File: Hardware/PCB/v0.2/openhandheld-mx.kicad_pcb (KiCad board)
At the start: 2 copper layers, 80 x 40 mm, 11 parts

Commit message: PCB v0.2: Completed schematic
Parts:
- removed the REF** at (19.8, -15.5)
- removed the REF** at (-30.0, -15.5)
- removed the REF** at (27.5, 1.00)
- removed the REF** at (-20.0, 16.0)
- removed the REF** at (20.0, 16.0)
- removed the REF** at (35.0, -15.0)
- removed the REF** at (-35.0, -15.0)
- removed the REF** at (0.00, 0.00)
- removed the S? at (33.5, -2.50)
- removed the S? at (23.5, 2.50)
- removed the VR at (-28.5, 0.00)
- added REF**: SJ-3524-SMT-TR, _AKL_Connector:SJ-3524-SMT-TR, B.Cu at (-12.0, -12.5)
- added REF**: MountingHole_2.2mm_M2_Pad, MountingHole:MountingHole_2.2mm_M2_Pad, F.Cu at (37.0, -16.0)
- added REF**: MountingHole_2.2mm_M2_Pad, MountingHole:MountingHole_2.2mm_M2_Pad, F.Cu at (20.5, 16.0)
- added REF**: MountingHole_2.2mm_M2_Pad, MountingHole:MountingHole_2.2mm_M2_Pad, F.Cu at (-20.5, 16.0)
- added REF**: MountingHole_2.2mm_M2_Pad, MountingHole:MountingHole_2.2mm_M2_Pad, F.Cu at (-37.0, -16.0)
- added REF**: PinSocket_2x05_P2.54mm_Vertical, Connector_PinSocket_2.54mm:PinSocket_2x05_P2.54mm_Vertical, F.Cu at (-30.1, -19.0)
- added REF**: Speaker_15x11mm, _AKL_Speaker:Speaker_15x11mm, B.Cu at (-32.5, 10.0)
- added REF**: ST7789_1.54_240x240, _AKL_Display:ST7789_1.54_240x240, F.Cu at (0.00, 0.00)
- added REF**: DFN-8-1EP_6x5mm_P1.27mm_EP2x2mm, Package_DFN_QFN:DFN-8-1EP_6x5mm_P1.27mm_EP2x2mm, B.Cu at (0.00, 8.50)
- added REF**: STM32-UFQFPN48, _AKL_IC:STM32-UFQFPN48, B.Cu at (0.00, 0.00)
- added REF**: PinSocket_2x06_P2.54mm_Vertical, Connector_PinSocket_2.54mm:PinSocket_2x06_P2.54mm_Vertical, F.Cu at (19.0, -26.0)
- added REF**: PinSocket_2x05_P2.54mm_Vertical, Connector_PinSocket_2.54mm:PinSocket_2x05_P2.54mm_Vertical, F.Cu at (19.9, -19.0)
- added REF**: BK-880, _AKL_Battery:BK-880, B.Cu at (29.0, 0.00)
- added S?: Button-SMD-6x6, _AKL_Switch:Button-SMD-6x6-Cap, F.Cu at (34.0, -2.50)
- added S?: Button-SMD-6x6, _AKL_Switch:Button-SMD-6x6-Cap, F.Cu at (24.0, 2.50)
- added VR: FJ08K-N, _AKL_ResistorVar:FJ08K-N, F.Cu at (-29.0, 0.00)
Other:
- board size 80 x 40 mm -> 84 x 42 mm
- board text added: "ONLY LIR2450"
- board text removed: "Dejar hueco en el acrilico para la pestaña central del conector SWD, como en la de nano 0"

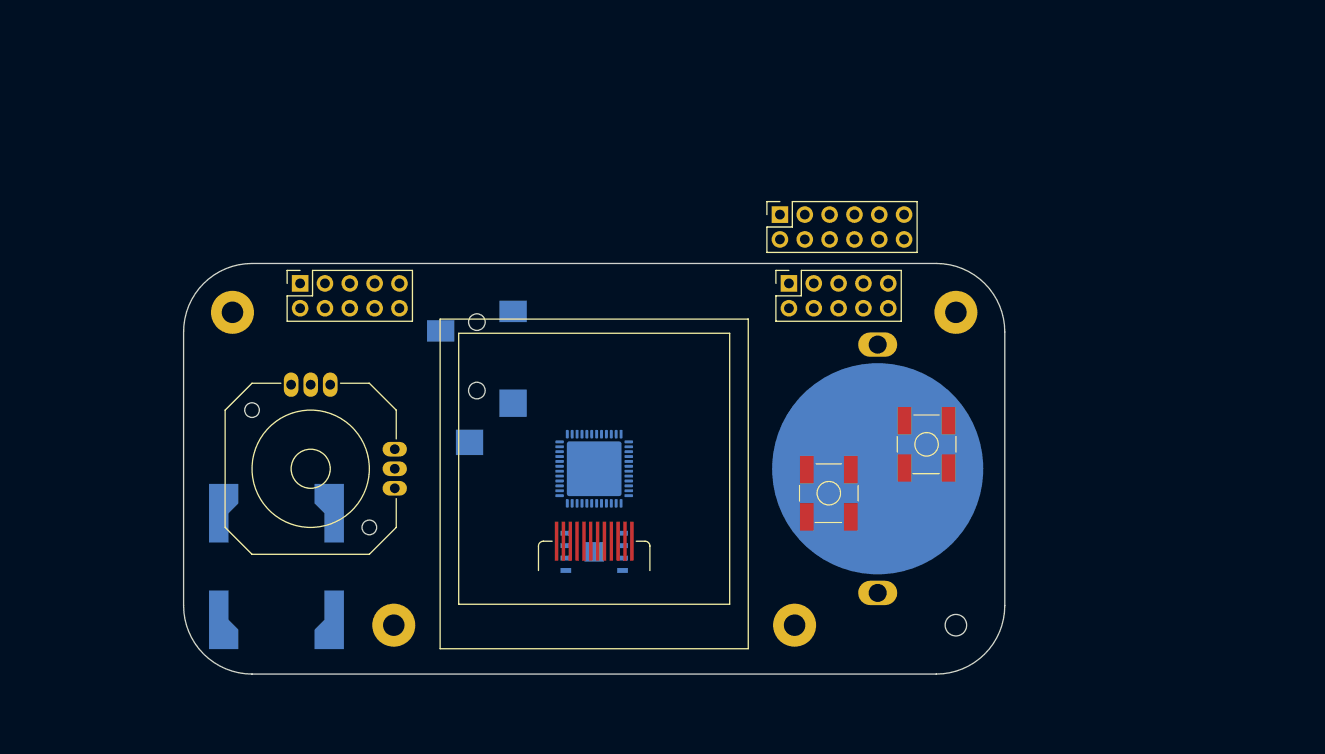
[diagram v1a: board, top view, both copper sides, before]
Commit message: PCB v0.2: Reduced component dimensions. Preliminary placement
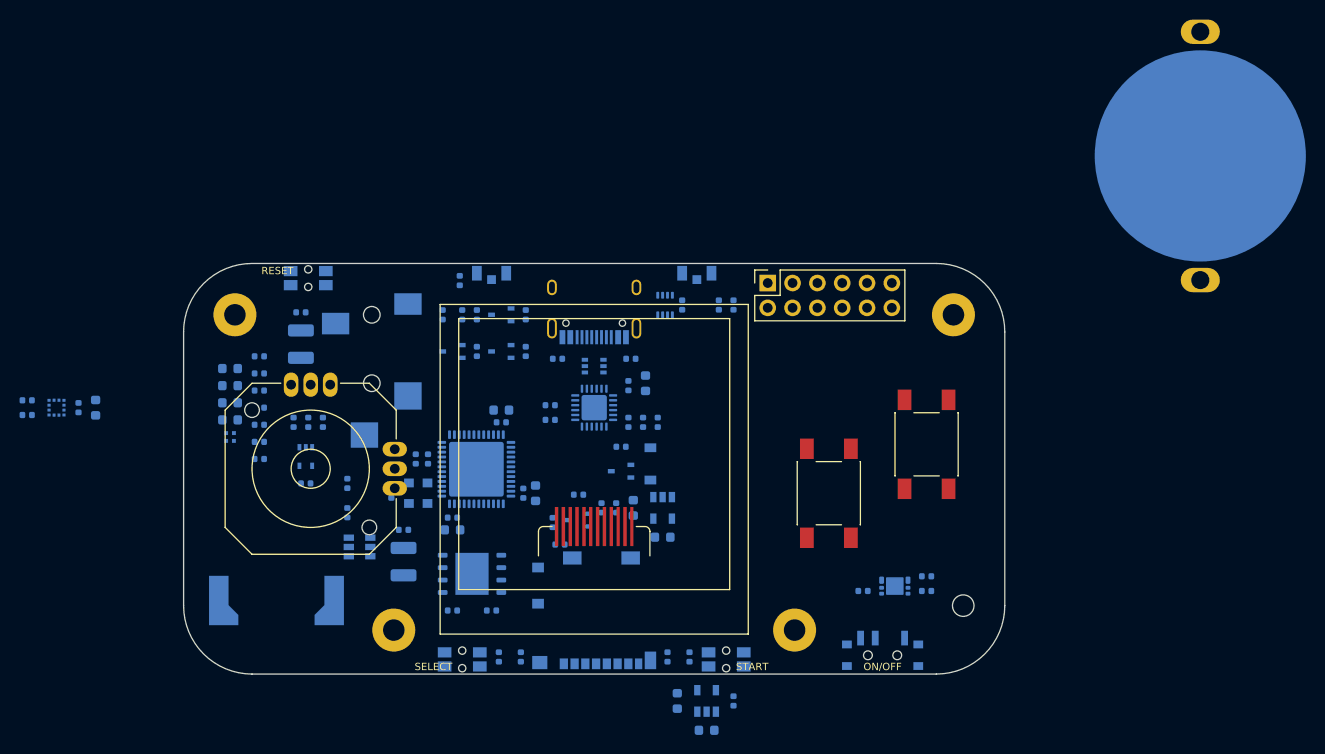
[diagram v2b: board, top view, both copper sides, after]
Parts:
- removed the REF** at (-12.0, -12.5)
- removed the REF** at (37.0, -16.0)
- removed the REF** at (20.5, 16.0)
- removed the REF** at (-30.1, -19.0)
- removed the REF** at (-32.5, 10.0)
- removed the REF** at (0.00, 0.00) (x2)
- removed the REF** at (0.00, 8.50)
- removed the REF** at (19.0, -26.0)
- removed the REF** at (19.9, -19.0)
- removed the REF** at (29.0, 0.00)
- removed S? (x2): Button-SMD-6x6, _AKL_Switch:Button-SMD-6x6-Cap
- removed VR: FJ08K-N, _AKL_ResistorVar:FJ08K-N
- added C1: 10uF, Capacitor_SMD:C_0603_1608Metric, B.Cu at (5.25, -8.75)
- added C10: 1uF, Capacitor_SMD:C_0402_1005Metric, B.Cu at (-18.2, -1.00)
- added C11: 100nF, Capacitor_SMD:C_0402_1005Metric, B.Cu at (-20.8, 2.50)
- added C12: 100nF, Capacitor_SMD:C_0402_1005Metric, B.Cu at (-17.0, -1.00)
- added C13: 10uF, Capacitor_SMD:C_0603_1608Metric, B.Cu at (-9.50, -6.00)
- added C14: 10uF, Capacitor_SMD:C_0603_1608Metric, B.Cu at (11.5, 26.8)
- added C15: 100nF, Capacitor_SMD:C_0402_1005Metric, B.Cu at (-9.50, -4.75)
- added C16: 1uF, Capacitor_SMD:C_0402_1005Metric, B.Cu at (-19.5, 6.25)
- added C17: 10uF, Capacitor_SMD:C_0603_1608Metric, B.Cu at (-6.00, 2.50)
- added C18: 100uF, Capacitor_SMD:C_1210_3225Metric, B.Cu at (-19.5, 9.50)
- added C19: 100nF, Capacitor_SMD:C_0402_1005Metric, B.Cu at (-7.25, 2.50)
- added C2: 100nF, Capacitor_SMD:C_0402_1005Metric, B.Cu at (3.50, -8.50)
- added C20: 10uF, Capacitor_SMD:C_0603_1608Metric, B.Cu at (-14.5, 6.25)
- added C21: 100nF, Capacitor_SMD:C_0402_1005Metric, B.Cu at (-14.5, 5.00)
- added C22: 100nF, Capacitor_SMD:C_0402_1005Metric, B.Cu at (34.0, 12.5)
- added C23: 10uF, Capacitor_SMD:C_0603_1608Metric, B.Cu at (-51.0, -6.25)
- added C24: 100nF, Capacitor_SMD:C_0402_1005Metric, B.Cu at (-52.8, -6.25)
- added C25: 100nF, Capacitor_SMD:C_0402_1005Metric, B.Cu at (-10.5, 14.5)
- added C26: 10uF, Capacitor_SMD:C_0603_1608Metric, B.Cu at (4.00, 4.00)
- added C27: 100nF, Capacitor_SMD:C_0402_1005Metric, B.Cu at (7.50, 19.2)
- added C28: 10uF, Capacitor_SMD:C_0603_1608Metric, B.Cu at (7.00, 7.00)
- added C29: 100nF, Capacitor_SMD:C_0402_1005Metric, B.Cu at (-4.25, 5.50)
- added C3: 100nF, Capacitor_SMD:C_0402_1005Metric, B.Cu at (-29.5, 1.50)
- added C4: 100nF, Capacitor_SMD:C_0402_1005Metric, B.Cu at (-13.5, -15.8)
- added C5: 100nF, Capacitor_SMD:C_0402_1005Metric, B.Cu at (-27.8, -4.75)
- added C6: 100uF, Capacitor_SMD:C_1210_3225Metric, B.Cu at (-30.0, -12.8)
- added C7: 10uF, Capacitor_SMD:C_0603_1608Metric, B.Cu at (8.50, 23.8)
- added C8: 100nF, Capacitor_SMD:C_0402_1005Metric, B.Cu at (-25.2, 1.50)
- added C9: 1uF, Capacitor_SMD:C_0402_1005Metric, B.Cu at (9.00, -16.8)
- added D1: PESD5V0L5UY, Package_TO_SOT_SMD:SOT-363_SC-70-6, B.Cu at (0.00, -10.5)
- added D2: BLUE, LED_SMD:LED_0603_1608Metric, B.Cu at (-37.2, -5.00)
- added D3: BLUE, LED_SMD:LED_0603_1608Metric, B.Cu at (-37.2, -6.75)
- added D4: RED, LED_SMD:LED_0603_1608Metric, B.Cu at (-37.2, -8.50)
- added D5: VEMD10940F, _AKL_Optical:Vishay_IR, B.Cu at (10.5, -20.0)
- added D6: VSMB10940, _AKL_Optical:Vishay_IR, B.Cu at (-10.5, -20.0)
- added D7: RGB, _AKL_Optical:150044M155260, B.Cu at (-37.2, -3.25)
- added D8: MBR0520L, Diode_SMD:D_SOD-123, B.Cu at (5.75, -0.50)
- added D9: GREEN, LED_SMD:LED_0603_1608Metric, B.Cu at (-37.2, -10.2)
- added DS1: ST7789_1.54_240x240, _AKL_Display:ST7789_1.54_240x240, F.Cu at (0.00, -1.50)
- added J1: TYPE-C-31-M-12, _AKL_Connector:TYPE-C-31-M-12, B.Cu at (0.00, -17.5)
- added J2: SJ-3524-SMT-TR, _AKL_Connector:SJ-3524-SMT-TR, B.Cu at (-22.8, -13.2)
- added J3: BK-880, _AKL_Battery:BK-880, B.Cu at (62.0, -32.0)
- added J4: 1040310811, _AKL_Connector:1040310811, B.Cu at (0.00, 14.5)
- added J5: PPPC062LFBN-RC, Connector_PinSocket_2.54mm:PinSocket_2x06_P2.54mm_Vertical, F.Cu at (17.8, -19.0)
- added LS1: CMS-151125-078S, _AKL_Speaker:Speaker_15x11mm, B.Cu at (-32.5, 8.50)
- added Q1: SI2102-TP, Package_TO_SOT_SMD:SOT-323_SC-70, B.Cu at (-9.50, -12.0)
- added Q2: SI2102-TP, Package_TO_SOT_SMD:SOT-323_SC-70, B.Cu at (-9.50, -15.8)
- added Q3: SI2102-TP, Package_TO_SOT_SMD:SOT-323_SC-70, B.Cu at (-14.5, -12.0)
- added Q4: SI2101-TP, Package_TO_SOT_SMD:SOT-323_SC-70, B.Cu at (2.75, 0.25)
- added Q5: SI2102-TP, Package_TO_SOT_SMD:SOT-323_SC-70, B.Cu at (-1.80, 5.25)
- added R1: 20K, Resistor_SMD:R_0402_1005Metric, B.Cu at (-7.00, -15.8)
- added R10: 20K, Resistor_SMD:R_0402_1005Metric, B.Cu at (-15.5, -15.8)
- added R11: 1K8, Resistor_SMD:R_0402_1005Metric, B.Cu at (-34.2, -6.25)
- added R12: 1K8, Resistor_SMD:R_0402_1005Metric, B.Cu at (-30.0, -16.0)
- added R13: 1K8, Resistor_SMD:R_0402_1005Metric, B.Cu at (-34.2, -8.00)
- added R14: 2K4, Resistor_SMD:R_0402_1005Metric, B.Cu at (-34.2, -9.75)
- added R15: 120K, Resistor_SMD:R_0402_1005Metric, B.Cu at (-25.2, 4.50)
- added R16: 20K, Resistor_SMD:R_0402_1005Metric, B.Cu at (14.2, 23.8)
- added R17: 5K1, Resistor_SMD:R_0402_1005Metric, B.Cu at (-4.50, -5.00)
- added R18: 150, Resistor_SMD:R_0402_1005Metric, B.Cu at (-13.8, -19.2)
- added R19: 5K1, Resistor_SMD:R_0402_1005Metric, B.Cu at (-4.50, -6.50)
- added R2: 20K, Resistor_SMD:R_0402_1005Metric, B.Cu at (-7.00, -12.0)
- added R20: 510, Resistor_SMD:R_0402_1005Metric, B.Cu at (34.0, 11.0)
- added R21: 2K4, Resistor_SMD:R_0402_1005Metric, B.Cu at (27.5, 12.5)
- added R22: 240, Resistor_SMD:R_0402_1005Metric, B.Cu at (-34.2, -4.50)
- added R23: 1K8, Resistor_SMD:R_0402_1005Metric, B.Cu at (-34.2, -2.75)
- added R24: 1K, Resistor_SMD:R_0402_1005Metric, B.Cu at (-34.2, -1.00)
- added R25: 120K, Resistor_SMD:R_0402_1005Metric, B.Cu at (2.75, -2.25)
- added R26: 20K, Resistor_SMD:R_0402_1005Metric, B.Cu at (-14.5, 14.5)
- added R27: 5K1, Resistor_SMD:R_0402_1005Metric, B.Cu at (-58.0, -5.50)
- added R28: 5K1, Resistor_SMD:R_0402_1005Metric, B.Cu at (-58.0, -7.00)
- added R29: 20K, Resistor_SMD:R_0402_1005Metric, B.Cu at (-7.50, 19.2)
- added R3: 1K, Resistor_SMD:R_0402_1005Metric, B.Cu at (3.50, -4.75)
- added R30: 20K, Resistor_SMD:R_0402_1005Metric, B.Cu at (-1.60, 2.65)
- added R31: 100, Resistor_SMD:R_0402_1005Metric, B.Cu at (-3.50, 7.75)
- added R32: 510, Resistor_SMD:R_0402_1005Metric, B.Cu at (-34.2, -11.5)
- added R33: 20K, Resistor_SMD:R_0402_1005Metric, B.Cu at (14.2, -16.8)
- added R34: 20K, Resistor_SMD:R_0402_1005Metric, B.Cu at (12.8, -16.8)
- added R35: 20K, Resistor_SMD:R_0402_1005Metric, B.Cu at (9.75, 19.2)
- added R36: 75K, Resistor_SMD:R_0402_1005Metric, B.Cu at (6.50, -4.75)
- added R37: 120K, Resistor_SMD:R_0402_1005Metric, B.Cu at (5.00, -4.75)
- added R38: 20K, Resistor_SMD:R_0402_1005Metric, B.Cu at (-9.75, 19.2)
- added R39: 75K, Resistor_SMD:R_0402_1005Metric, B.Cu at (2.25, 4.00)
- added R4: 5K1, Resistor_SMD:R_0402_1005Metric, B.Cu at (3.75, -11.2)
- added R40: 120K, Resistor_SMD:R_0402_1005Metric, B.Cu at (0.75, 4.00)
- added R5: 5K1, Resistor_SMD:R_0402_1005Metric, B.Cu at (-3.75, -11.2)
- added R6: 20K, Resistor_SMD:R_0402_1005Metric, B.Cu at (-12.0, -12.0)
- added R7: 20K, Resistor_SMD:R_0402_1005Metric, B.Cu at (-12.0, -15.8)
- added R8: 240, Resistor_SMD:R_0402_1005Metric, B.Cu at (-30.8, -4.75)
- added R9: 100, Resistor_SMD:R_0402_1005Metric, B.Cu at (-29.2, -4.75)
- added REF**: MountingHole_2.2mm_M2_Pad, MountingHole:MountingHole_2.2mm_M2_Pad, F.Cu at (36.8, -15.8)
- added REF**: MountingHole_2.2mm_M2_Pad, MountingHole:MountingHole_2.2mm_M2_Pad, F.Cu at (20.5, 16.5)
- added SW1: RESET, _AKL_Switch:EVQP7, B.Cu at (-29.2, -19.5)
- added SW2: ON/OFF, _AKL_Switch:CUS-12TB, B.Cu at (29.5, 18.8)
- added SW3: A, _AKL_Switch:TL3301TF160QG, F.Cu at (24.0, 2.50)
- added SW4: B, _AKL_Switch:TL3301TF160QG, F.Cu at (34.0, -2.50)
- added SW5: START, _AKL_Switch:EVQP7, B.Cu at (13.5, 19.5)
- added SW6: SELECT, _AKL_Switch:EVQP7, B.Cu at (-13.5, 19.5)
- added U1: TLV9061IDCKR, Package_TO_SOT_SMD:SOT-353_SC-70-5, B.Cu at (-29.5, -1.25)
- added U10: LIS2DE12TR, _AKL_IC:LIS2DE12TR, B.Cu at (-55.0, -6.25)
- added U11: TLV74333PDBVR, Package_TO_SOT_SMD:SOT-23-5, B.Cu at (7.00, 4.00)
- added U2: CP2102N-A02-GQFN24, Package_DFN_QFN:QFN-24-1EP_4x4mm_P0.5mm_EP2.6x2.6mm, B.Cu at (0.00, -6.25)
- added U3: MCP73831T-2ACI_OT, Package_TO_SOT_SMD:SOT-23-5, B.Cu at (11.5, 23.8)
- added U4: PAM8301AAF, Package_TO_SOT_SMD:SOT-23-6, B.Cu at (-24.0, 8.00)
- added U5: DSC6001CI1A-008.0000T, _AKL_IC:DSC60XX-3.2x2.5, B.Cu at (-18.0, 2.50)
- added U6: VSOP38338, _AKL_IC:VSOP38338, B.Cu at (7.25, -16.8)
- added U7: AP9211S-AN-HAC-7, _AKL_IC:AP9211S-AN-HAC-7, B.Cu at (30.8, 12.0)
- added U8: STM32L431CCU6, _AKL_IC:STM32-UFQFPN48, B.Cu at (-12.1, 0.05)
- added U9: W25Q64JVZPIQ, _AKL_IC:Winbond_WSON8_6x5mm, B.Cu at (-12.5, 10.8)
- added VR1: FJ08K-N, _AKL_ResistorVar:FJ08K-N, F.Cu at (-29.0, 0.00)
- moved REF** 0.50 mm to (-20.5, 16.5)
- moved REF** 0.35 mm to (-36.8, -15.8)
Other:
- outline, holes or cut-outs redrawn
- rule pad_to_mask_clearance: 0.051 -> 0
- board text added: "CHG"
- board text added: "ON/OFF"
- board text added: "PWR"
- board text added: "RESET"
- board text added: "RXD"
- board text added: "SELECT"
- board text added: "START"
- board text added: "TXD"
- board text added: "USR"

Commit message: PCB v0.2: Starting to route
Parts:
- D8: value MBR0520L -> NSR0520V2T1G; footprint Diode_SMD:D_SOD-123 -> Diode_SMD:D_SOD-523
- J3: value BK-880 -> Battery; footprint _AKL_Battery:BK-880 -> _AKL_Battery:Solder_Pad_D2
- moved J3 55.1 mm to (28.5, 11.8), turned to 180 degrees
- moved R27 44.7 mm to (-13.5, -9.25)
- moved R28 44.6 mm to (-13.5, -10.5)
- moved U10 44.1 mm to (-11.0, -9.75)
- moved C24 43.9 mm to (-9.00, -9.75)
- moved C23 43.6 mm to (-7.50, -9.75)
- moved C14 40.7 mm to (7.50, -13.8), turned to 180 degrees
- moved R16 40.3 mm to (11.8, -16.5)
- moved U3 40.3 mm to (9.25, -16.5)
- moved C7 40.3 mm to (6.50, -16.5)
- moved R30 18.0 mm to (10.2, 16.2), turned to 90 degrees
- moved Q5 14.7 mm to (8.25, 16.0), turned to 90 degrees
- moved C11 13.1 mm to (-12.2, -7.50), turned to 0 degrees
- moved R31 13.0 mm to (8.25, 13.2), turned to 270 degrees
- moved C15 10.3 mm to (-5.00, 4.50), turned to 270 degrees
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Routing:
- net GND: track 0.00 -> 35.1 mm, vias 0 -> 33
- net /SPEAKER_-: track 0.00 -> 17.1 mm
- net /3V3: track 0.00 -> 15.2 mm, vias 0 -> 17
- net /LEDK: track 0.00 -> 11.7 mm, vias 0 -> 2
- net /SPEAKER_+: track 0.00 -> 9.63 mm
- net /BTN_B: track 0.00 -> 9.10 mm
- net /BTN_A: track 0.00 -> 9.10 mm
- net /AUD6: track 0.00 -> 8.67 mm
- net /VCC: track 0.00 -> 8.22 mm, vias 0 -> 4
- net /SPI2_NSS: track 0.00 -> 6.51 mm
- net /BTN_START: track 0.00 -> 5.82 mm
- net /LED_RX: track 0.00 -> 5.56 mm
- net /BTN_SELECT: track 0.00 -> 5.52 mm
- net /RGB_R: track 0.00 -> 5.43 mm
- net /RESET: track 0.00 -> 5.31 mm, vias 0 -> 1
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- added copper zone on In2.Cu, net (none)
- added copper zone on B.Cu, net /3V3
- added copper zone on B.Cu, net /VCC
- added copper zone on B.Cu, net GND
- added copper zone on F.Cu, net GND
- added copper zone on In2.Cu, net GND
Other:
- copper layers 2 -> 4
- net class Default: via_dia 0.8 -> 0.7; via_drill 0.4 -> 0.3
- rule via_min_size: 0.4 -> 0.7
- board text removed: "ONLY LIR2450"

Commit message: PCB v0.2: Finished placement, created power planes
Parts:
- moved R28 29.6 mm to (15.0, -18.5), turned to 270 degrees
- moved R27 28.8 mm to (13.8, -18.5), turned to 270 degrees
- moved U3 21.0 mm to (6.55, 4.35)
- moved C14 20.9 mm to (6.30, 7.10), turned to 0 degrees
- moved U10 19.0 mm to (7.50, -14.0), turned to 270 degrees
- moved R16 18.3 mm to (8.35, 1.45), turned to 90 degrees
- moved C7 18.1 mm to (6.30, 1.60), turned to 0 degrees
- moved C24 15.6 mm to (6.50, -11.2), turned to 270 degrees
- moved C23 15.6 mm to (8.00, -11.0), turned to 270 degrees
- moved C28 11.2 mm to (-2.75, 0.50), turned to 270 degrees
- moved R34 9.78 mm to (15.0, -15.5), turned to 90 degrees
- moved R33 7.79 mm to (13.8, -15.5), turned to 90 degrees
- moved U11 7.38 mm to (0.00, 0.50), turned to 180 degrees
- moved C9 6.86 mm to (7.50, -17.2), turned to 90 degrees
- moved R40 4.35 mm to (-1.00, -2.00), turned to 180 degrees
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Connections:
- D1 pad 3: /USB_DM -> /USB_DP
- D1 pad 4: /USB_DP -> /USB_DM
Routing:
- net GND: track 35.1 -> 98.9 mm, vias 33 -> 70
- net /VCC: track 8.22 -> 50.0 mm, vias 4 -> 9
- net /3V3: track 15.2 -> 46.1 mm, vias 17 -> 36
- net /RTS: track 0.00 -> 19.5 mm
- net /RESET: track 5.31 -> 22.7 mm, vias 1 -> 0
- net /DTR: track 0.00 -> 16.8 mm
- net /VUSB: track 0.72 -> 15.3 mm, vias 1 -> 15
- net /AUD1: track 0.00 -> 13.0 mm
- net /USB_DP: track 0.00 -> 12.4 mm
- net /USB_DM: track 0.00 -> 11.1 mm, vias 0 -> 2
- net /VBAT: track 0.00 -> 10.6 mm, vias 0 -> 12
- net /I2C1_SCL: track 0.00 -> 8.69 mm
- net /I2C1_SDA: track 0.00 -> 8.41 mm
- net /CC1: track 0.00 -> 5.27 mm
- net /CC2: track 0.00 -> 5.06 mm
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- added copper zone on F.Cu, net /3V3
- added copper zone on In1.Cu, net /3V3
- added copper zone on B.Cu, net /AUD2
- added copper zone on B.Cu, net /AUD3
- added copper zone on B.Cu, net /BAT_GND
- added copper zone on B.Cu, net /LEDK
- added copper zone on B.Cu, net /VBAT
- added copper zone on In1.Cu, net /VBAT
- added copper zone on In1.Cu, net /VCC
- added copper zone on B.Cu, net /VUSB
- added copper zone on In1.Cu, net /VUSB
- removed copper zone on In2.Cu, net (none)

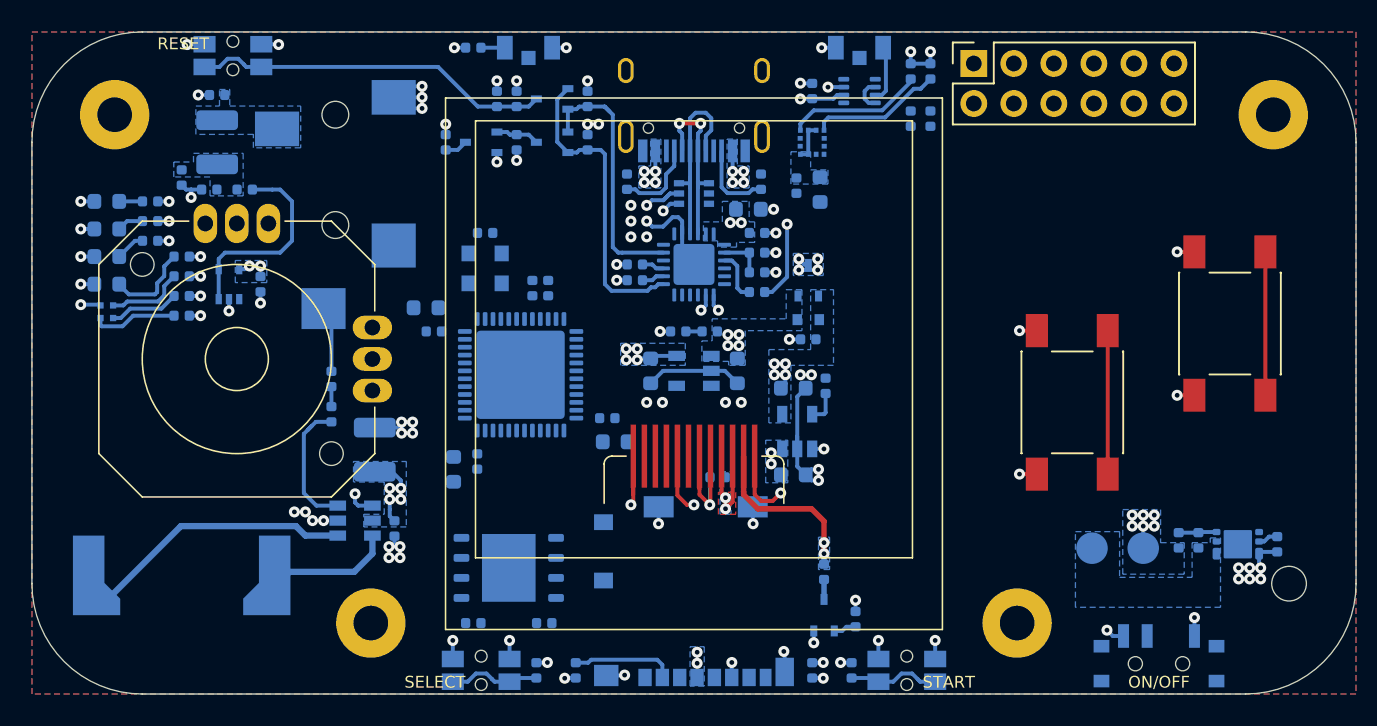
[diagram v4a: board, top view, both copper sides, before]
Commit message: PCB v0.2: Power planes
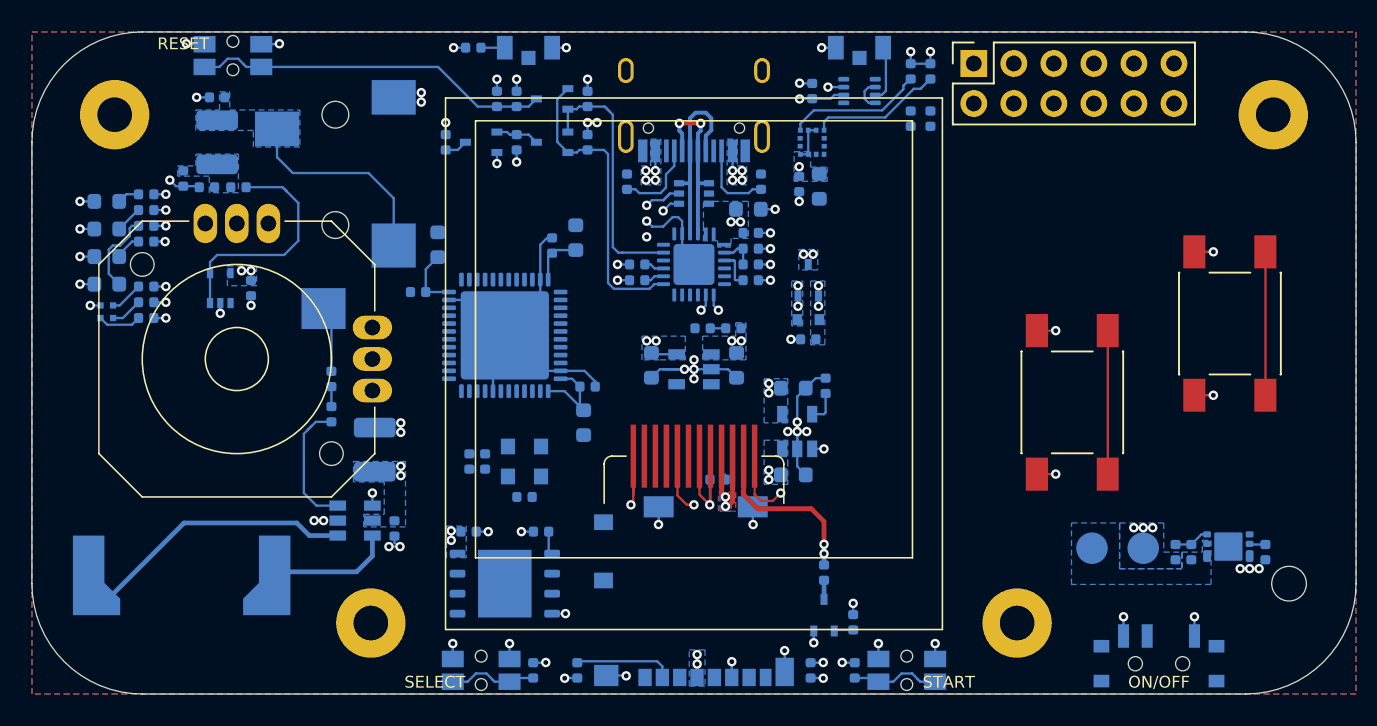
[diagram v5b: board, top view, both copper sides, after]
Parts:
- moved C11 16.9 mm to (-10.8, 8.50), turned to 180 degrees
- moved C13 16.8 mm to (-16.2, -7.50), turned to 90 degrees
- moved C17 16.6 mm to (-7.50, -7.95), turned to 90 degrees
- moved C19 14.5 mm to (-9.00, -7.45), turned to 90 degrees
- moved C15 14.4 mm to (-17.5, -4.50), turned to 180 degrees
- moved U5 12.5 mm to (-10.8, 6.25), turned to 90 degrees
- moved C20 12.4 mm to (-7.00, 3.79), turned to 270 degrees
- moved C10 12.1 mm to (-14.2, 6.25), turned to 270 degrees
- moved C12 11.4 mm to (-13.2, 6.25), turned to 270 degrees
- moved C21 10.4 mm to (-6.75, 1.50), turned to 0 degrees
- moved C25 7.53 mm to (-14.3, 10.7), turned to 0 degrees
- moved R26 7.22 mm to (-9.70, 10.7), turned to 0 degrees
- moved R11 2.98 mm to (-34.8, -8.70)
- moved U8 2.69 mm to (-12.0, -1.75), turned to 90 degrees
- moved R22 2.34 mm to (-34.8, -4.85)
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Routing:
- net /VCC: track 50.0 -> 5.24 mm, vias 9 -> 7
- net /AUD3: track 0.00 -> 13.3 mm
- net /VBAT: track 10.6 -> 0.23 mm, vias 12 -> 7
- net /VUSB: track 15.3 -> 6.40 mm
- net GND: track 98.9 -> 106.2 mm, vias 70 -> 59
- net /3V3: track 46.1 -> 49.6 mm, vias 36 -> 38
- net /RGB_B: track 4.97 -> 2.11 mm
- net /RGB_R: track 5.43 -> 2.77 mm
- net /RGB_G: track 4.44 -> 2.03 mm
- net /AUD1: track 13.0 -> 15.1 mm
- net /QSPI_NCS: track 0.00 -> 1.48 mm
- net /VUSB_DET: track 2.83 -> 2.28 mm
- removed copper zone on B.Cu, net /LEDK
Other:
- net class Default: clearance 0.2 -> 0.15; trace_width 0.25 -> 0.15; via_dia 0.7 -> 0.6
- rule trace_clearance: 0.2 -> 0.15
- rule trace_min: 0.2 -> 0.15
- rule via_min_size: 0.7 -> 0.6
